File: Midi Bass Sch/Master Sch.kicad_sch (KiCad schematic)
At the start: 31 parts, among them J1 DIN-5, J2 Master ISCP, SW2 Master Reset, U1 PIC16F1788

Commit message: began working on pcb for project
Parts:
- SW1: footprint (none) -> Connector_PinHeader_2.54mm:PinHeader_1x05_P2.54mm_Vertical
- SW2: footprint (none) -> Button_Switch_THT:SW_PUSH_6mm_H5mm
- TP1, TP2, TP3, TP4: footprint (none) -> Connector_PinHeader_2.54mm:PinHeader_1x01_P2.54mm_Vertical
- U1: footprint (none) -> OF footprints:SSOP-28
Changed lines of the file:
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@@
 			)
 		)
-		(property "Footprint" ""
+		(property "Footprint" "Connector_PinHeader_2.54mm:PinHeader_1x01_P2.54mm_Vertical"
 			(at 168.91 69.85 0)
 			(effects
@@
 			)
 		)
-		(property "Footprint" ""
+		(property "Footprint" "Connector_PinHeader_2.54mm:PinHeader_1x05_P2.54mm_Vertical"
 			(at 29.21 142.24 0)
 			(effects
@@
 			)
 		)
-		(property "Footprint" ""
+		(property "Footprint" "Connector_PinHeader_2.54mm:PinHeader_1x01_P2.54mm_Vertical"
 			(at 168.91 29.21 0)
 			(effects
@@
 			)
 		)
-		(property "Footprint" ""
+		(property "Footprint" "OF footprints:SSOP-28"
 			(at 130.81 52.07 0)
 			(effects
@@
 			)
 		)
-		(property "Footprint" ""
+		(property "Footprint" "Connector_PinHeader_2.54mm:PinHeader_1x01_P2.54mm_Vertical"
 			(at 55.88 114.3 0)
 			(effects
@@
 			)
 		)
-		(property "Footprint" ""
+		(property "Footprint" "Connector_PinHeader_2.54mm:PinHeader_1x01_P2.54mm_Vertical"
 			(at 179.07 63.5 0)
 			(effects
@@
 			)
 		)
-		(property "Footprint" ""
+		(property "Footprint" "Button_Switch_THT:SW_PUSH_6mm_H5mm"
 			(at 58.42 25.4 0)
 			(effects

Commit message: started basic pcb layout for Master pic
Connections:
- net at C1.1, R5.1, SW2.2: now also D5.2; no longer D5.1
- net at J2.1, U1.1 (RE3/~{MCLR}/Vpp): now also D5.1; no longer D5.2

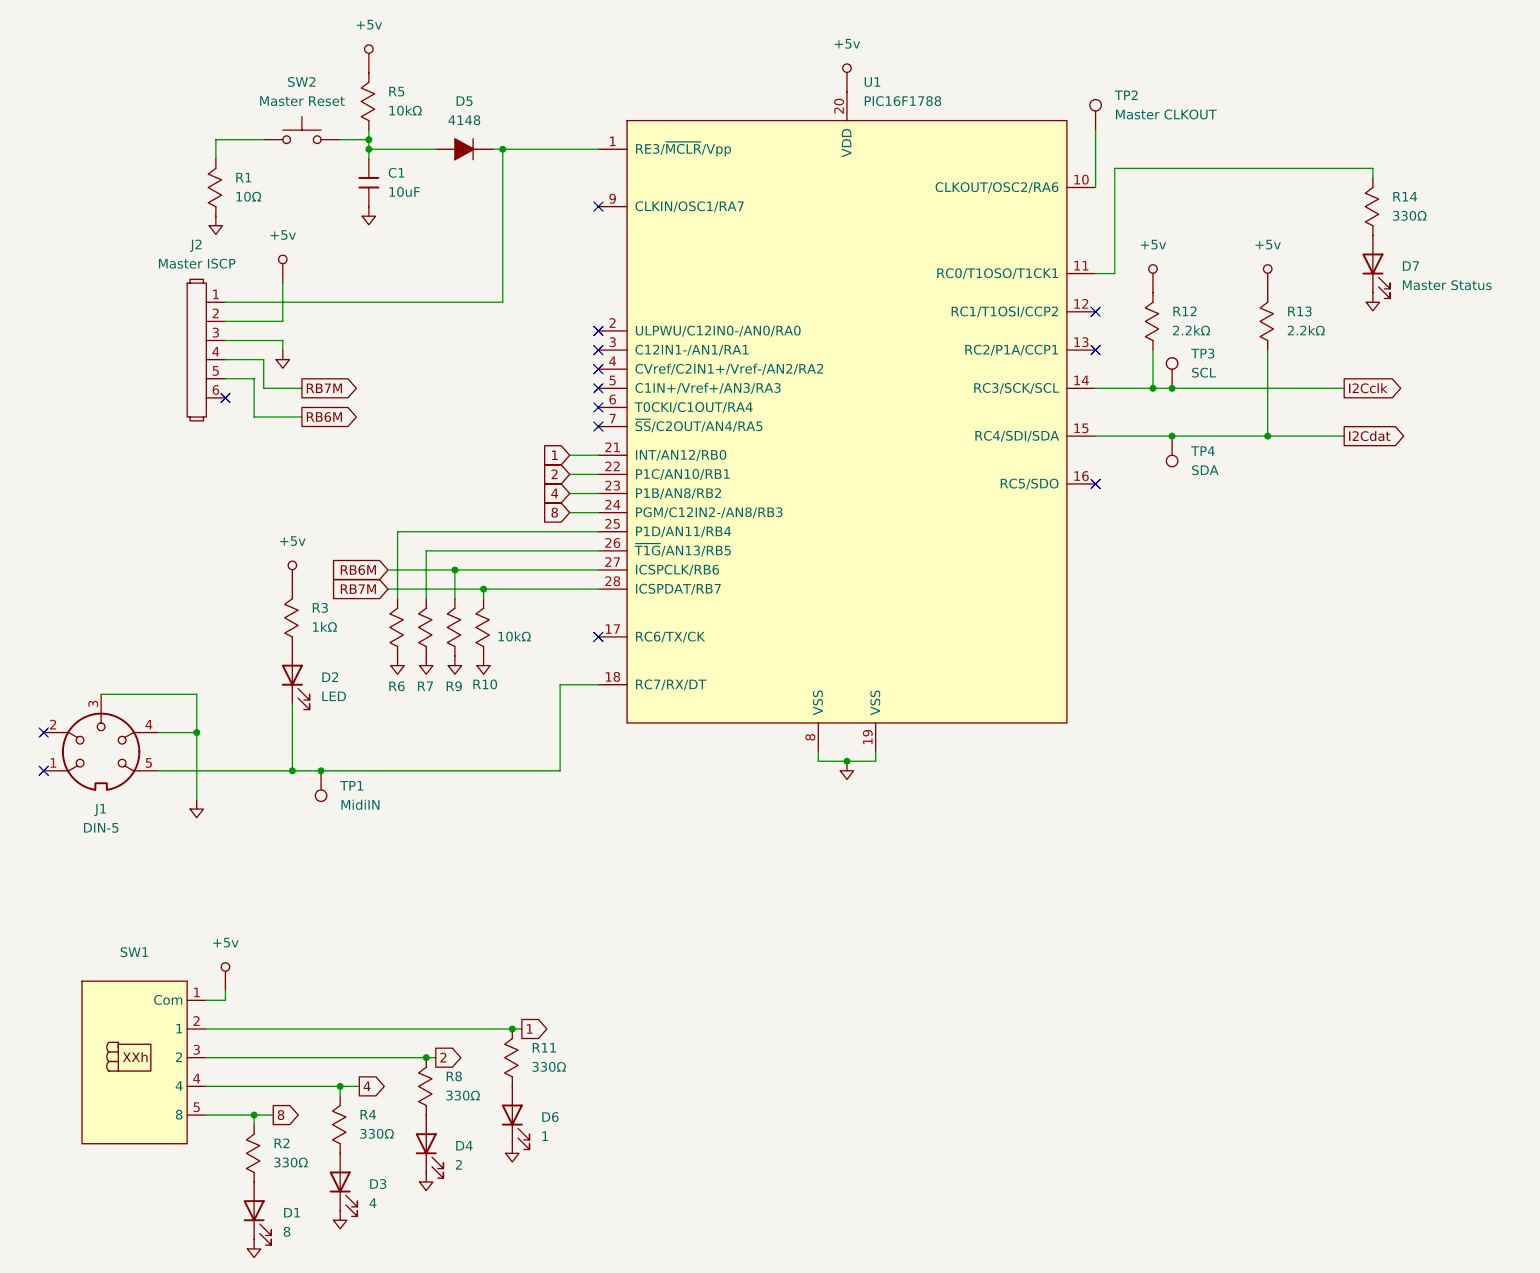
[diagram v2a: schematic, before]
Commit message: working on final troubleshooting sections, modified pluck slave to header connections
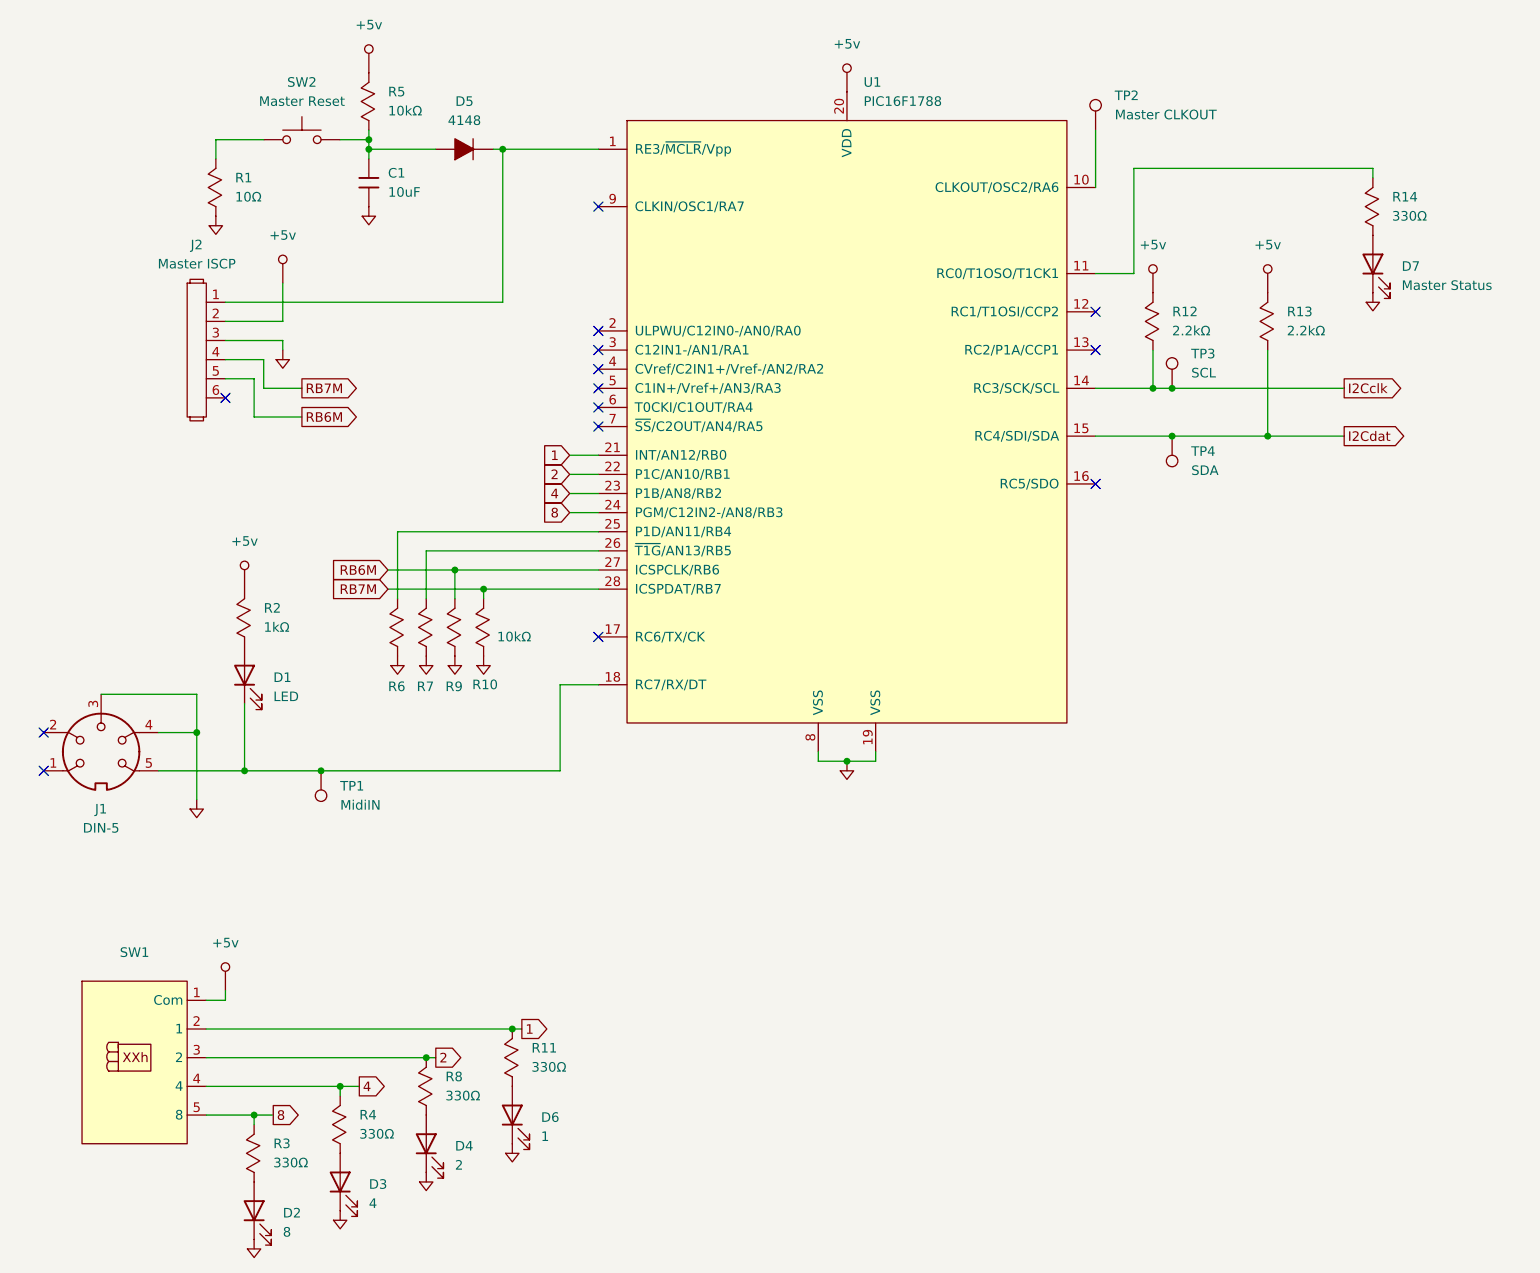
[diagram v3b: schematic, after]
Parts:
- renumbered D2 to D1, D1 to D2, R3 to R2, R2 to R3
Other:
- moved on the sheet: D1, R2
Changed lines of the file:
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@@
 	)
 	(junction
-		(at 67.31 31.75)
+		(at 50.8 114.3)
 		(diameter 0)
 		(color 0 0 0 0)
 	)
 	(junction
-		(at 186.69 69.85)
+		(at 67.31 31.75)
 		(diameter 0)
 		(color 0 0 0 0)
 	)
 	(junction
-		(at 60.96 114.3)
+		(at 186.69 69.85)
 		(diameter 0)
 		(color 0 0 0 0)
 	)
 	(junction
-		(at 86.36 148.59)
+		(at 60.96 114.3)
 		(diameter 0)
 		(color 0 0 0 0)
 	)
 	(junction
-		(at 57.15 114.3)
+		(at 86.36 148.59)
 		(diameter 0)
 		(color 0 0 0 0)
@@
 	(wire
 		(pts
-			(xy 166.37 48.26) (xy 166.37 34.29)
+			(xy 168.91 48.26) (xy 168.91 34.29)
 		)
 		(stroke
@@
 	(wire
 		(pts
-			(xy 57.15 114.3) (xy 60.96 114.3)
-		)
-		(stroke
-			(width 0)
-			(type default)
-		)
-	)
-	(wire
-		(pts
 			(xy 92.71 114.3) (xy 92.71 102.87)
 		)
@@
 	(wire
 		(pts
-			(xy 39.37 114.3) (xy 57.15 114.3)
+			(xy 39.37 114.3) (xy 50.8 114.3)
 		)
 		(stroke
@@
 	(wire
 		(pts
-			(xy 57.15 105.41) (xy 57.15 114.3)
+			(xy 50.8 105.41) (xy 50.8 114.3)
 		)
 		(stroke
@@
 	(wire
 		(pts
-			(xy 166.37 34.29) (xy 200.66 34.29)
+			(xy 168.91 34.29) (xy 200.66 34.29)
 		)
 		(stroke
@@
 	(wire
 		(pts
+			(xy 50.8 114.3) (xy 60.96 114.3)
+		)
+		(stroke
+			(width 0)
+			(type default)
+		)
+	)
+	(wire
+		(pts
 			(xy 173.99 63.5) (xy 171.45 63.5)
 		)
@@
 	(wire
 		(pts
-			(xy 163.83 48.26) (xy 166.37 48.26)
+			(xy 163.83 48.26) (xy 168.91 48.26)
 		)
 		(stroke
@@
 		(dnp no)
 		(fields_autoplaced yes)
-		(property "Reference" "R2"
+		(property "Reference" "R3"
 			(at 54.61 163.8299 90)
 			(effects
@@
 			(project "Midi Bass Sch"
 				(path "/06818073-fb22-48ee-acc5-6dedd827034e/0dc3b915-e001-48bd-b9bb-7010249087fd"
-					(reference "R2")
+					(reference "R3")
 					(unit 1)
 				)
@@
 	(symbol
 		(lib_id "Device:LED")
-		(at 57.15 101.6 90)
+		(at 50.8 101.6 90)
 		(unit 1)
 		(exclude_from_sim no)
@@
 		(dnp no)
 		(fields_autoplaced yes)
-		(property "Reference" "D2"
-			(at 60.96 101.9174 90)
+		(property "Reference" "D1"
+			(at 54.61 101.9174 90)
 			(effects
 				(font
@@
 		)
 		(property "Value" "LED"
-			(at 60.96 104.4574 90)
+			(at 54.61 104.4574 90)
 			(effects
 				(font
@@
 		)
 		(property "Footprint" "Diode_SMD:D_0805_2012Metric_Pad1.15x1.40mm_HandSolder"
-			(at 57.15 101.6 0)
+			(at 50.8 101.6 0)
 			(effects
 				(font
@@
 		)
 		(property "Datasheet" "~"
-			(at 57.15 101.6 0)
+			(at 50.8 101.6 0)
 			(effects
 				(font
@@
 		)
 		(property "Description" "Light emitting diode"
-			(at 57.15 101.6 0)
+			(at 50.8 101.6 0)
 			(effects
 				(font
@@
 			(project "Midi Bass Sch"
 				(path "/06818073-fb22-48ee-acc5-6dedd827034e/0dc3b915-e001-48bd-b9bb-7010249087fd"
-					(reference "D2")
+					(reference "D1")
 					(unit 1)
 				)
@@
 		(dnp no)
 		(fields_autoplaced yes)
-		(property "Reference" "#PWR04"
+		(property "Reference" "#PWR05"
 			(at 52.07 175.26 0)
 			(effects
@@
 			(project "Midi Bass Sch"
 				(path "/06818073-fb22-48ee-acc5-6dedd827034e/0dc3b915-e001-48bd-b9bb-7010249087fd"
-					(reference "#PWR04")
+					(reference "#PWR05")
 					(unit 1)
 				)
@@
 		(dnp no)
 		(fields_autoplaced yes)
-		(property "Reference" "#PWR06"
+		(property "Reference" "#PWR07"
 			(at 55.88 57.15 0)
 			(effects
@@
 			(project "Midi Bass Sch"
 				(path "/06818073-fb22-48ee-acc5-6dedd827034e/0dc3b915-e001-48bd-b9bb-7010249087fd"
-					(reference "#PWR06")
+					(reference "#PWR07")
 					(unit 1)
 				)
@@
 	(symbol
 		(lib_id "Owen's Symbols:Resistor_Mod")
-		(at 57.15 93.98 90)
+		(at 50.8 93.98 90)
 		(unit 1)
 		(exclude_from_sim no)
@@
 		(dnp no)
 		(fields_autoplaced yes)
-		(property "Reference" "R3"
-			(at 59.69 92.7099 90)
+		(property "Reference" "R2"
+			(at 53.34 92.7099 90)
 			(effects
 				(font
@@
 		)
 		(property "Value" "1kΩ"
-			(at 59.69 95.2499 90)
+			(at 53.34 95.2499 90)
 			(effects
 				(font
@@
 		)
 		(property "Footprint" "Resistor_SMD:R_0805_2012Metric_Pad1.20x1.40mm_HandSolder"
-			(at 54.61 95.25 0)
+			(at 48.26 95.25 0)
 			(effects
 				(font
@@
 		)
 		(property "Datasheet" ""
-			(at 54.61 95.25 0)
+			(at 48.26 95.25 0)
 			(effects
 				(font
@@
 		)
 		(property "Description" ""
-			(at 57.15 93.98 0)
+			(at 50.8 93.98 0)
 			(effects
 				(font
@@
 			(project "Midi Bass Sch"
 				(path "/06818073-fb22-48ee-acc5-6dedd827034e/0dc3b915-e001-48bd-b9bb-7010249087fd"
-					(reference "R3")
+					(reference "R2")
 					(unit 1)
 				)
@@
 		(dnp no)
 		(fields_autoplaced yes)
-		(property "Reference" "D1"
+		(property "Reference" "D2"
 			(at 55.88 173.0374 90)
 			(effects
@@
 			(project "Midi Bass Sch"
 				(path "/06818073-fb22-48ee-acc5-6dedd827034e/0dc3b915-e001-48bd-b9bb-7010249087fd"
-					(reference "D1")
+					(reference "D2")
 					(unit 1)
 				)
@@
 	(symbol
 		(lib_id "Custom Power:+5v")
-		(at 57.15 88.9 0)
+		(at 50.8 88.9 0)
 		(unit 1)
 		(exclude_from_sim no)
@@
 		(dnp no)
 		(fields_autoplaced yes)
-		(property "Reference" "#PWR07"
-			(at 61.8744 85.1916 0)
+		(property "Reference" "#PWR04"
+			(at 55.5244 85.1916 0)
 			(effects
 				(font
@@
 		)
 		(property "Value" "+5v"
-			(at 57.15 83.82 0)
+			(at 50.8 83.82 0)
 			(effects
 				(font
@@
 		)
 		(property "Footprint" ""
-			(at 57.15 85.09 0)
+			(at 50.8 85.09 0)
 			(effects
 				(font
@@
 		)
 		(property "Datasheet" ""
-			(at 57.15 85.09 0)
+			(at 50.8 85.09 0)
 			(effects
 				(font
@@
 		)
 		(property "Description" ""
-			(at 57.15 88.9 0)
+			(at 50.8 88.9 0)
 			(effects
 				(font
@@
 			(project "Midi Bass Sch"
 				(path "/06818073-fb22-48ee-acc5-6dedd827034e/0dc3b915-e001-48bd-b9bb-7010249087fd"
-					(reference "#PWR07")
+					(reference "#PWR04")
 					(unit 1)
 				)
@@
 		(dnp no)
 		(fields_autoplaced yes)
-		(property "Reference" "#PWR05"
+		(property "Reference" "#PWR06"
 			(at 60.6044 44.5516 0)
 			(effects
@@
 			(project "Midi Bass Sch"
 				(path "/06818073-fb22-48ee-acc5-6dedd827034e/0dc3b915-e001-48bd-b9bb-7010249087fd"
-					(reference "#PWR05")
+					(reference "#PWR06")
 					(unit 1)
 				)

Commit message: began getting images for schematic appendix
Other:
- title: (none) -> Master Schematic
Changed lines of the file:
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@@
 	(generator_version "8.0")
 	(paper "A")
+	(title_block
+		(title "Master Schematic")
+		(date "2024-12-10")
+		(rev "A")
+	)
 	(junction
 		(at 44.45 109.22)

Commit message: began working on pcb layout deleted extra schematics for solenoid break out board
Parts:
- TP4: footprint Connector_PinHeader_2.54mm:PinHeader_1x01_P2.54mm_Vertical -> Connector_PinHeConnector_PinHeader_2.54mm:PinHeader_1x01_P2.54mm_Verticalader_2.54mm:PinHeader_1x01_P2.54mm_Vertical
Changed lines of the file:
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@@
 			)
 		)
-		(property "Footprint" "Connector_PinHeader_2.54mm:PinHeader_1x01_P2.54mm_Vertical"
+		(property "Footprint" "Connector_PinHeConnector_PinHeader_2.54mm:PinHeader_1x01_P2.54mm_Verticalader_2.54mm:PinHeader_1x01_P2.54mm_Vertical"
 			(at 168.91 69.85 0)
 			(effects

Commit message: created pcb for breakout working on pcb for main control board
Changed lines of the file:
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@@
 (kicad_sch
-	(version 20231120)
+	(version 20250114)
 	(generator "eeschema")
-	(generator_version "8.0")
+	(generator_version "9.0")
 	(paper "A")
 	(title_block

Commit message: created and generated Rev. B of Motherboard
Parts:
- J1: footprint (none) -> OF Footprints:Din_5 Connector
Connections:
- net GND: now also J1.2; no longer J1.3
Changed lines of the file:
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@@
 	)
 	(no_connect
-		(at 24.13 109.22)
+		(at 31.75 104.14)
 	)
 	(no_connect
@@
 	(wire
 		(pts
+			(xy 44.45 101.6) (xy 44.45 109.22)
+		)
+		(stroke
+			(width 0)
+			(type default)
+		)
+	)
+	(wire
+		(pts
 			(xy 186.69 69.85) (xy 186.69 58.42)
 		)
@@
 	(wire
 		(pts
-			(xy 186.69 69.85) (xy 196.85 69.85)
+			(xy 20.32 101.6) (xy 44.45 101.6)
 		)
 		(stroke
@@
 	(wire
 		(pts
-			(xy 60.96 114.3) (xy 92.71 114.3)
+			(xy 186.69 69.85) (xy 196.85 69.85)
 		)
 		(stroke
@@
 	(wire
 		(pts
-			(xy 74.93 152.4) (xy 76.2 152.4)
+			(xy 60.96 114.3) (xy 92.71 114.3)
 		)
 		(stroke
@@
 	(wire
 		(pts
-			(xy 196.85 63.5) (xy 173.99 63.5)
+			(xy 74.93 152.4) (xy 76.2 152.4)
 		)
 		(stroke
@@
 	(wire
 		(pts
-			(xy 48.26 57.15) (xy 55.88 57.15)
+			(xy 196.85 63.5) (xy 173.99 63.5)
 		)
 		(stroke
@@
 	(wire
 		(pts
-			(xy 52.07 67.31) (xy 52.07 62.23)
+			(xy 48.26 57.15) (xy 55.88 57.15)
 		)
 		(stroke
@@
 	(wire
 		(pts
-			(xy 82.55 91.44) (xy 82.55 90.17)
+			(xy 52.07 67.31) (xy 52.07 62.23)
 		)
 		(stroke
@@
 	(wire
 		(pts
-			(xy 78.74 87.63) (xy 97.79 87.63)
+			(xy 82.55 91.44) (xy 82.55 90.17)
 		)
 		(stroke
@@
 	(wire
 		(pts
-			(xy 44.45 104.14) (xy 44.45 109.22)
+			(xy 78.74 87.63) (xy 97.79 87.63)
 		)
 		(stroke
@@
 	(wire
 		(pts
+			(xy 20.32 109.22) (xy 20.32 101.6)
+		)
+		(stroke
+			(width 0)
+			(type default)
+		)
+	)
+	(wire
+		(pts
 			(xy 45.72 148.59) (xy 86.36 148.59)
 		)
@@
 	(wire
 		(pts
-			(xy 53.34 63.5) (xy 58.42 63.5)
+			(xy 24.13 109.22) (xy 20.32 109.22)
 		)
 		(stroke
@@
 	(wire
 		(pts
-			(xy 52.07 160.02) (xy 54.61 160.02)
+			(xy 53.34 63.5) (xy 58.42 63.5)
 		)
 		(stroke
@@
 	(wire
 		(pts
-			(xy 93.98 80.01) (xy 97.79 80.01)
+			(xy 52.07 160.02) (xy 54.61 160.02)
 		)
 		(stroke
@@
 	(wire
 		(pts
-			(xy 31.75 104.14) (xy 44.45 104.14)
+			(xy 93.98 80.01) (xy 97.79 80.01)
 		)
 		(stroke
@@
 			)
 		)
-		(property "Footprint" ""
+		(property "Footprint" "OF Footprints:Din_5 Connector"
 			(at 31.75 111.76 0)
 			(effects
